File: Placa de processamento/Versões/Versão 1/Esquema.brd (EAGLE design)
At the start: 145.1 x 79.8 mm, 15 parts, among them IC2 5V

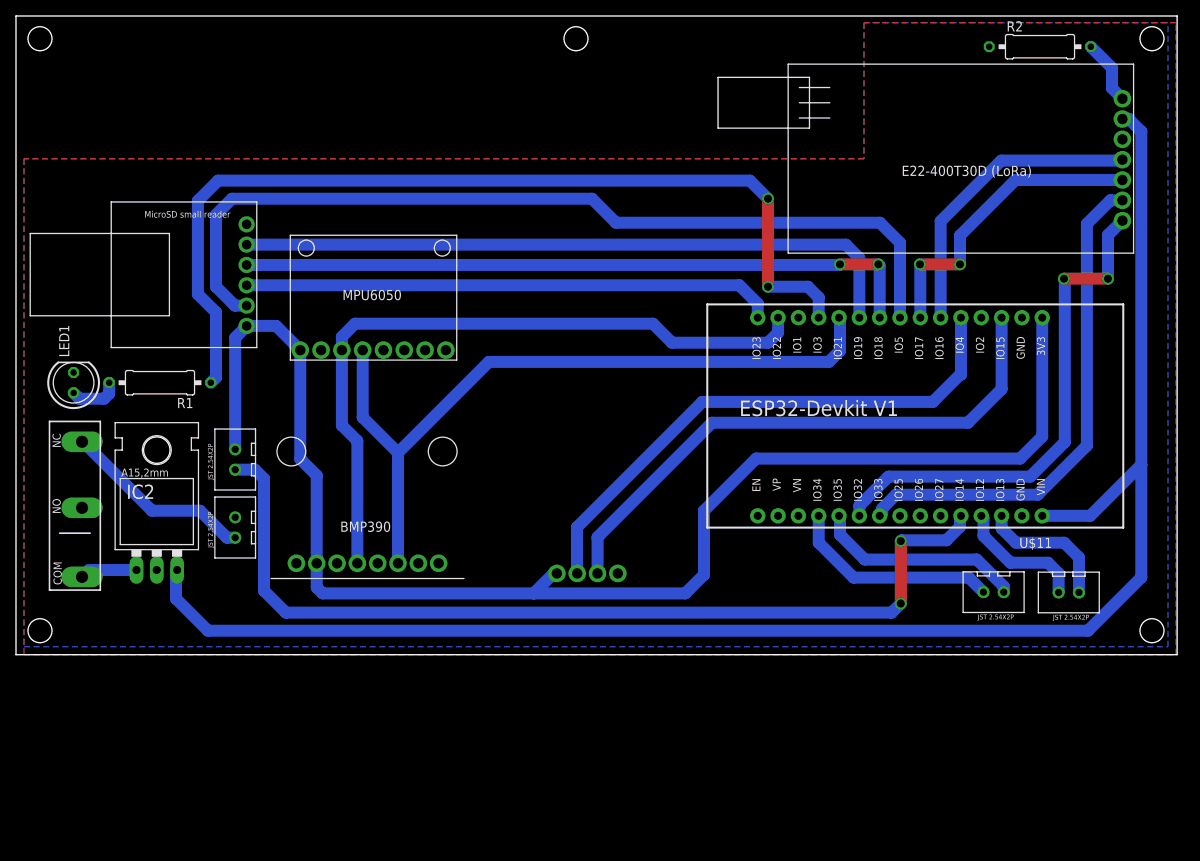
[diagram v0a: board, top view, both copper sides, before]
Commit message: mudanças na placa de processamento
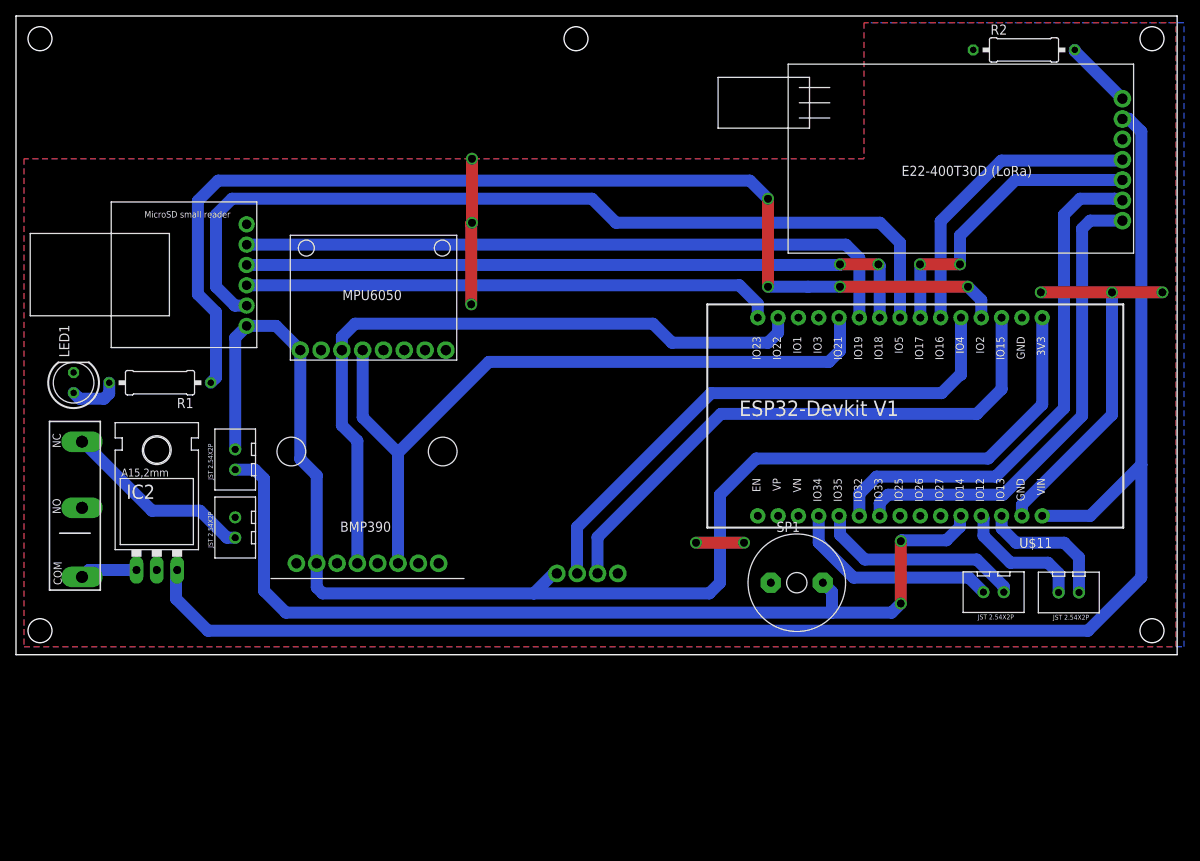
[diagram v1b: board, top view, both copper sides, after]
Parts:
- added SP1: AL60P, buzzer:AL60P
- R2: value 40R -> 46R
- moved R2 2.04 mm to (126.0, 75.6)
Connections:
- net BUZZER: now also SP1.2
- net GND: now also SP1.1, U$11.29
- net LED1: now also U$11.4; no longer U$11.12
- net M0: now also U$11.22; no longer U$11.21
- net M1: now also U$11.21; no longer U$11.22
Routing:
- net GND: track 0.00 -> 72.0 mm, vias 0 -> 8
- net LED1: track 117.6 -> 137.7 mm, vias 2 -> 4
- net BUZZER: track 116.6 -> 120.8 mm
- net M0: track 64.3 -> 60.3 mm, vias 2 -> 0
- net M1: track 63.3 -> 65.2 mm
- net 3V3: track 177.1 -> 176.5 mm

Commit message: teste
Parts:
- moved IC2 0.76 mm to (18.3, 14.1)
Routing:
- net VIN: track 7.16 -> 8.70 mm
- net V_BATTERY: track 24.1 -> 25.0 mm
- net VOUT: track 202.6 -> 201.9 mm
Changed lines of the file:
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@@
 <drawing>
 <settings>
-<setting alwaysvectorfont="no"/>
+<setting alwaysvectorfont="yes"/>
 <setting verticaltext="up"/>
 </settings>
@@
 </class>
 </classes>
-<designrules name="padronizacao do eagle *">
+<designrules name="default *">
 <description language="de">&lt;b&gt;EAGLE Design Rules&lt;/b&gt;
 &lt;p&gt;
@@
 <param name="msMicroVia" value="9.99mm"/>
 <param name="msBlindViaRatio" value="0.5"/>
-<param name="rvPadTop" value="0.35"/>
+<param name="rvPadTop" value="0.25"/>
 <param name="rvPadInner" value="0.25"/>
-<param name="rvPadBottom" value="0.35"/>
+<param name="rvPadBottom" value="0.25"/>
 <param name="rvViaOuter" value="0.25"/>
 <param name="rvViaInner" value="0.25"/>
 <param name="rvMicroViaOuter" value="0.25"/>
 <param name="rvMicroViaInner" value="0.25"/>
-<param name="rlMinPadTop" value="10mil"/>
+<param name="rlMinPadTop" value="20mil"/>
 <param name="rlMaxPadTop" value="30mil"/>
 <param name="rlMinPadInner" value="10mil"/>
 <param name="rlMaxPadInner" value="20mil"/>
-<param name="rlMinPadBottom" value="10mil"/>
+<param name="rlMinPadBottom" value="20mil"/>
 <param name="rlMaxPadBottom" value="30mil"/>
-<param name="rlMinViaOuter" value="8mil"/>
-<param name="rlMaxViaOuter" value="20mil"/>
-<param name="rlMinViaInner" value="8mil"/>
-<param name="rlMaxViaInner" value="20mil"/>
+<param name="rlMinViaOuter" value="22mil"/>
+<param name="rlMaxViaOuter" value="22mil"/>
+<param name="rlMinViaInner" value="10mil"/>
+<param name="rlMaxViaInner" value="10mil"/>
 <param name="rlMinMicroViaOuter" value="4mil"/>
 <param name="rlMaxMicroViaOuter" value="20mil"/>
@@
 <param name="srMinRoundness" value="0mil"/>
 <param name="srMaxRoundness" value="0mil"/>
-<param name="slThermalIsolate" value="10mil"/>
+<param name="slThermalIsolate" value="0mil"/>
 <param name="slThermalsForVias" value="0"/>
 <param name="dpMaxLengthDifference" value="10mm"/>
@@
 <attribute name="NAME" x="129.54" y="14.62" size="1.27" layer="21" rot="R180"/>
 </element>
-<element name="IC2" library="v-reg" library_urn="urn:adsk.eagle:library:409" package="78XXL" package3d_urn="urn:adsk.eagle:package:30361/1" value="5V" x="17.6" y="14.4" smashed="yes">
-<attribute name="NAME" x="13.79" y="19.48" size="1.778" layer="25" ratio="10"/>
-<attribute name="POPULARITY" value="10" x="17.6" y="14.4" size="1.778" layer="27" display="off"/>
-<attribute name="VALUE" x="13.663" y="16.94" size="1.778" layer="27" ratio="10"/>
+<element name="IC2" library="v-reg" library_urn="urn:adsk.eagle:library:409" package="78XXL" package3d_urn="urn:adsk.eagle:package:30361/1" value="5V" x="18.3" y="14.1" smashed="yes">
+<attribute name="NAME" x="14.49" y="19.18" size="1.778" layer="25" ratio="10"/>
+<attribute name="POPULARITY" value="10" x="18.3" y="14.1" size="1.778" layer="27" display="off"/>
+<attribute name="VALUE" x="14.363" y="16.64" size="1.778" layer="27" ratio="10"/>
 </element>
 <element name="LED1" library="led" library_urn="urn:adsk.eagle:library:259" package="LED5MM" package3d_urn="urn:adsk.eagle:package:15799/2" value="RED" x="7.2" y="34" smashed="yes" rot="R90">
@@
 <attribute name="VALUE" x="21.175" y="34.6858" size="1.27" layer="27" ratio="10" rot="R180"/>
 </element>
-<element name="U$12" library="CRD" library_urn="urn:adsk.eagle:library:39051337" package="CHAVESS-5GL" package3d_urn="urn:adsk.eagle:package:45208058/6" value="CHAVE_SS-5GL" x="8" y="19" smashed="yes" rot="R90"/>
+<element name="U$12" library="CRD" library_urn="urn:adsk.eagle:library:39051337" package="CHAVESS-5GL" package3d_urn="urn:adsk.eagle:package:45208058/14" value="CHAVE_SS-5GL" x="8" y="19" smashed="yes" rot="R90"/>
 <element name="R2" library="rcl" library_urn="urn:adsk.eagle:library:334" package="0309/12" package3d_urn="urn:adsk.eagle:package:23571/1" value="46R" x="126" y="75.6" smashed="yes">
 <attribute name="NAME" x="121.809" y="77.505" size="1.27" layer="25" ratio="10"/>
@@
 <contactref element="U$12" pad="P$1"/>
 <contactref element="IC2" pad="IN"/>
-<wire x1="8.254" y1="9.729" x2="9.115" y2="10.59" width="1.5" layer="16"/>
-<wire x1="9.115" y1="10.59" x2="15.06" y2="10.59" width="1.5" layer="16"/>
+<wire x1="7.238" y1="9.856" x2="10.856" y2="9.856" width="3.7" layer="16"/>
+<wire x1="11" y1="10" x2="10.856" y2="9.856" width="3.7" layer="16"/>
+<wire x1="15.76" y1="10.29" x2="15.47" y2="10" width="1.5" layer="16"/>
+<wire x1="15.47" y1="10" x2="11" y2="10" width="1.5" layer="16"/>
 </signal>
 <signal name="V_BATTERY">
 <contactref element="U$7" pad="1"/>
 <contactref element="U$12" pad="P$3"/>
-<wire x1="8.254" y1="26.62" x2="8.38" y2="26.62" width="1.5" layer="16"/>
-<wire x1="17" y1="18" x2="23" y2="18" width="1.5" layer="16"/>
 <wire x1="23" y1="18" x2="26.37" y2="14.63" width="1.5" layer="16"/>
 <wire x1="26.37" y1="14.63" x2="27.4" y2="14.63" width="1.5" layer="16"/>
-<wire x1="8.38" y1="26.62" x2="17" y2="18" width="1.5" layer="16"/>
+<wire x1="9.2385" y1="24.2385" x2="10.2385" y2="23.2385" width="1.5" layer="16"/>
+<wire x1="7.238" y1="26.239" x2="9.2385" y2="24.2385" width="3.7" layer="16"/>
+<wire x1="10.2385" y1="23.2385" x2="11.7615" y2="23.2385" width="1.5" layer="16"/>
+<wire x1="11.7615" y1="23.2385" x2="17" y2="18" width="1.5" layer="16"/>
+<wire x1="17" y1="18" x2="23" y2="18" width="1.5" layer="16"/>
 </signal>
 <signal name="GND">
@@
 <via x="128.1" y="45.3" extent="1-16" drill="1"/>
 <wire x1="137" y1="30" x2="137" y2="45.3" width="1.5" layer="16"/>
-<wire x1="137" y1="45.3" x2="143.3" y2="45.3" width="1.5" layer="1"/>
-<via x="143.3" y="45.3" extent="1-16" drill="1"/>
+<wire x1="137" y1="45.3" x2="143" y2="45.3" width="1.5" layer="1"/>
+<via x="143" y="45.3" extent="1-16" drill="1"/>
 </signal>
 <signal name="N$4">
@@
 <wire x1="140.666" y1="23.746" x2="140.666" y2="9.666" width="1.5" layer="16"/>
 <wire x1="140.666" y1="9.666" x2="134" y2="3" width="1.5" layer="16"/>
-<wire x1="134" y1="3" x2="24" y2="3" width="1.5" layer="16"/>
-<wire x1="24" y1="3" x2="20" y2="7" width="1.5" layer="16"/>
-<wire x1="20" y1="7" x2="20" y2="10.45" width="1.5" layer="16"/>
-<wire x1="20" y1="10.45" x2="20.14" y2="10.59" width="1.5" layer="16"/>
+<wire x1="24" y1="3" x2="134" y2="3" width="1.5" layer="16"/>
+<wire x1="20.84" y1="10.29" x2="20.84" y2="6.16" width="1.5" layer="16"/>
+<wire x1="20.84" y1="6.16" x2="24" y2="3" width="1.5" layer="16"/>
 </signal>
 <signal name="N$7">

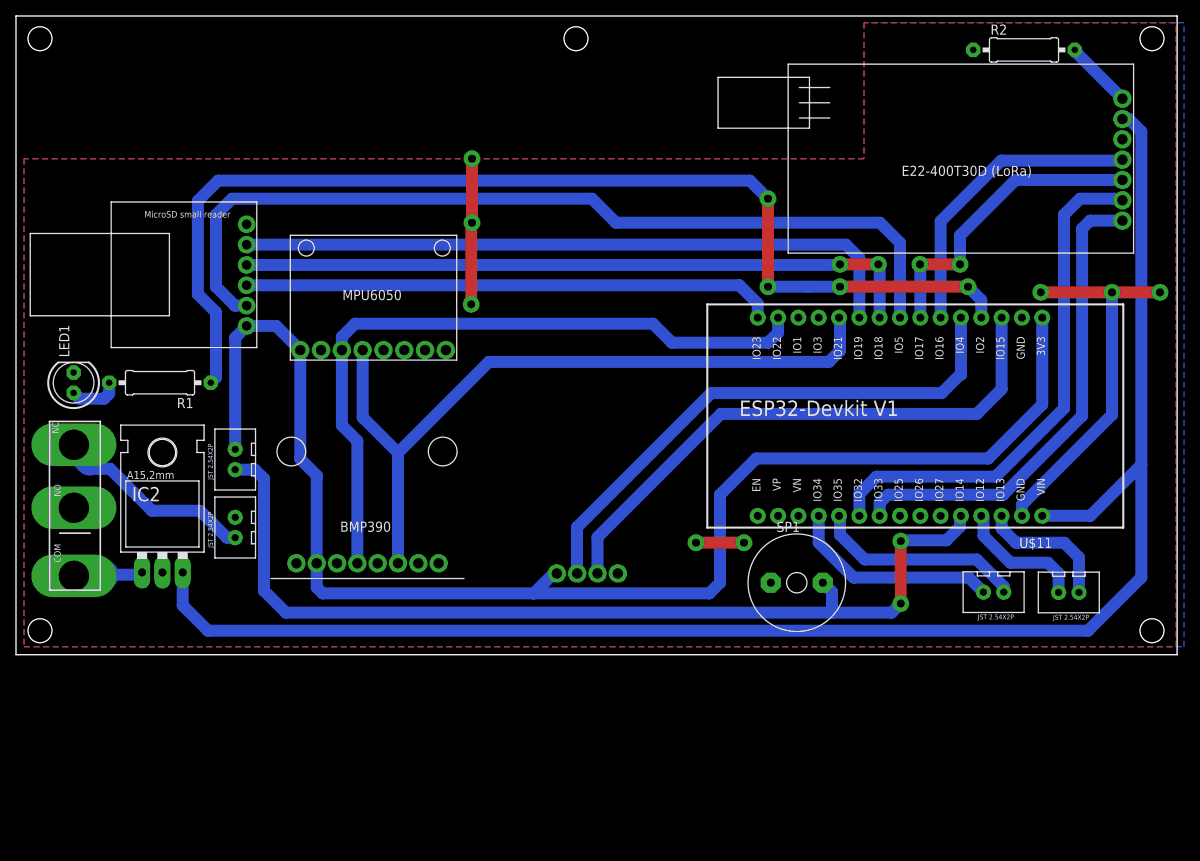
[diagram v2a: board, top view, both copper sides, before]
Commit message: atualização de regulador
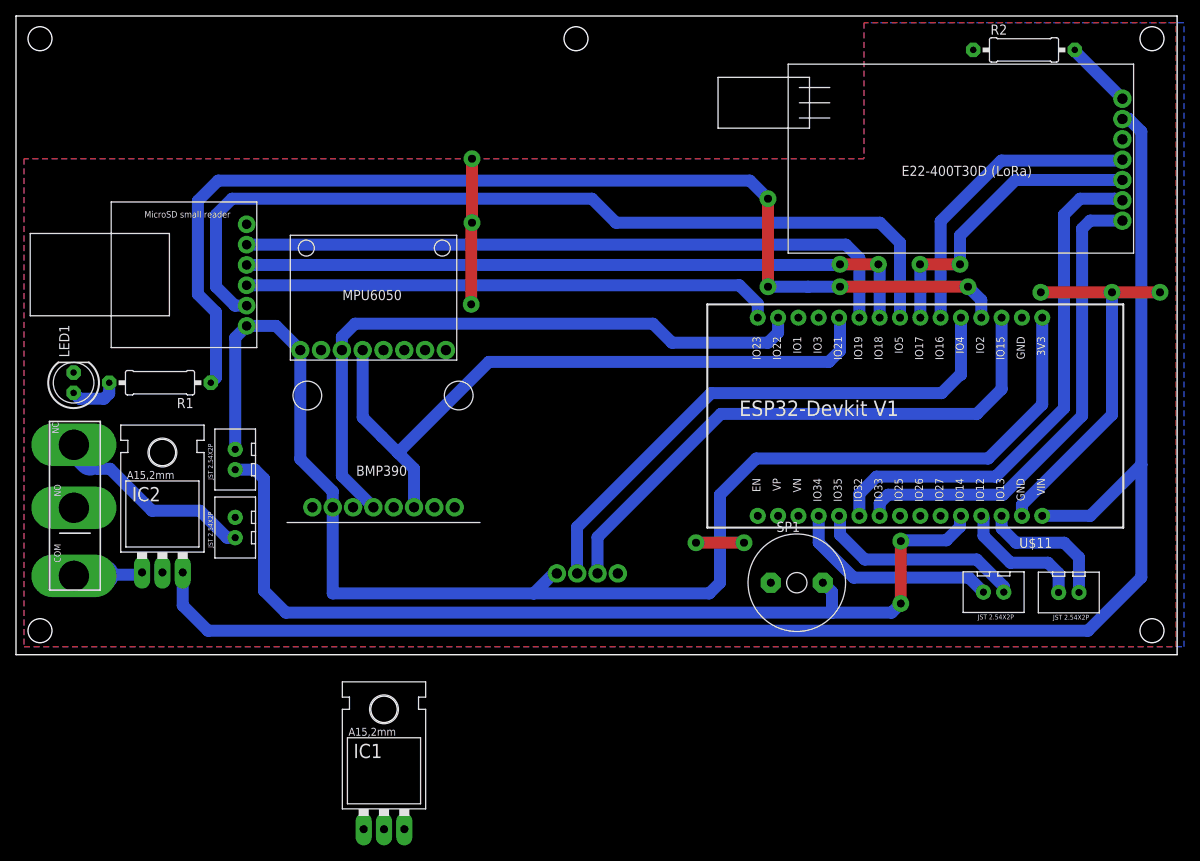
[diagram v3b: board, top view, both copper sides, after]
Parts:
- added IC1: 5V, v-reg:78XXL
- moved U$1 7.28 mm to (45.6, 26.8)
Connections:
- new net VOUT_LORA: IC1.OUT, U$2.VCC
- net GND: now also IC1.GND
- net VIN: now also IC1.IN
- net VOUT: no longer U$2.VCC
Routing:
- net SDA: track 93.2 -> 87.0 mm
- net SCL: track 87.7 -> 81.5 mm
- net 3V3: track 176.5 -> 175.8 mm
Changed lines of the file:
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@@
 </autorouter>
 <elements>
-<element name="U$1" library="CRD" library_urn="urn:adsk.eagle:library:39051337" package="BMP390_FOOTPRINT" package3d_urn="urn:adsk.eagle:package:40965124/5" value="BMP390V1" x="43.561" y="19.812" smashed="yes"/>
+<element name="U$1" library="CRD" library_urn="urn:adsk.eagle:library:39051337" package="BMP390_FOOTPRINT" package3d_urn="urn:adsk.eagle:package:40965124/5" value="BMP390V1" x="45.561" y="26.812" smashed="yes"/>
 <element name="U$2" library="CRD" library_urn="urn:adsk.eagle:library:39051337" package="E22-400T30D_FOOTPRINT" package3d_urn="urn:adsk.eagle:package:40965099/5" value="E22-400T30D" x="121.92" y="63.66" smashed="yes" rot="R180"/>
 <element name="U$3" library="CRD" library_urn="urn:adsk.eagle:library:39051337" package="GPS_MODULE_FOOTPRINT" package3d_urn="urn:adsk.eagle:package:39608400/7" value="GPS_MODULE" x="71.22" y="26.67" smashed="yes" rot="MR0"/>
@@
 <attribute name="VALUE" x="93.7138" y="5.19" size="1.27" layer="27" ratio="10"/>
 </element>
+<element name="IC1" library="v-reg" library_urn="urn:adsk.eagle:library:409" package="78XXL" package3d_urn="urn:adsk.eagle:package:30361/1" value="5V" x="46" y="-18" smashed="yes">
+<attribute name="NAME" x="42.19" y="-12.92" size="1.778" layer="25" ratio="10"/>
+<attribute name="POPULARITY" value="10" x="46" y="-18" size="1.778" layer="27" display="off"/>
+<attribute name="VALUE" x="42.063" y="-15.46" size="1.778" layer="27" ratio="10"/>
+</element>
 </elements>
 <signals>
@@
 <wire x1="15.76" y1="10.29" x2="15.47" y2="10" width="1.5" layer="16"/>
 <wire x1="15.47" y1="10" x2="11" y2="10" width="1.5" layer="16"/>
+<contactref element="IC1" pad="IN"/>
+<wire x1="7.238" y1="9.856" x2="43.46" y2="-21.81" width="0" layer="19" extent="1-1"/>
 </signal>
 <signal name="V_BATTERY">
@@
 <wire x1="137" y1="45.3" x2="143" y2="45.3" width="1.5" layer="1"/>
 <via x="143" y="45.3" extent="1-16" drill="1"/>
+<contactref element="IC1" pad="GND"/>
+<wire x1="128.1" y1="45.3" x2="119.65" y2="75.6" width="0" layer="19" extent="1-1"/>
+<wire x1="125.74" y1="42.13" x2="128.1" y2="45.3" width="0" layer="19" extent="1-1"/>
+<wire x1="94.3488" y1="9" x2="125.74" y2="17.36" width="0" layer="19" extent="1-1"/>
+<wire x1="91" y1="14" x2="94.3488" y2="9" width="0" layer="19" extent="1-1"/>
+<wire x1="75.23" y1="10.16" x2="85" y2="14" width="0" layer="19" extent="1-1"/>
+<wire x1="42.132" y1="18.43" x2="75.23" y2="10.16" width="0" layer="19" extent="1-1"/>
+<wire x1="27.4" y1="17.17" x2="42.132" y2="18.43" width="0" layer="19" extent="1-1"/>
+<wire x1="18.3" y1="10.29" x2="27.4" y2="17.17" width="0" layer="19" extent="1-1"/>
+<wire x1="38.1355" y1="38.0755" x2="27.4" y2="17.17" width="0" layer="19" extent="1-1"/>
+<wire x1="28.829" y1="53.8" x2="38.1355" y2="38.0755" width="0" layer="19" extent="1-1"/>
+<wire x1="56.9" y1="43.8" x2="38.1355" y2="38.0755" width="0" layer="19" extent="1-1"/>
+<wire x1="7.2" y1="35.27" x2="27.4" y2="17.17" width="0" layer="19" extent="1-1"/>
+<wire x1="46" y1="-21.81" x2="18.3" y2="10.29" width="0" layer="19" extent="1-1"/>
 </signal>
 <signal name="N$4">
@@
 <contactref element="U$11" pad="30"/>
 <contactref element="IC2" pad="OUT"/>
-<contactref element="U$2" pad="VCC"/>
 <wire x1="139.1" y1="66.9667875" x2="139.1" y2="67" width="1.5" layer="16"/>
 <wire x1="140.666" y1="65.4007875" x2="139.1" y2="66.9667875" width="1.5" layer="16"/>
@@
 <wire x1="140.666" y1="65.4007875" x2="140.666" y2="23.746" width="1.5" layer="16"/>
 <wire x1="139.1" y1="67" x2="138.341" y2="67" width="1.5" layer="16"/>
-<wire x1="138.341" y1="67" x2="138.303" y2="66.962" width="1.5" layer="16"/>
 <wire x1="140.666" y1="23.746" x2="140.666" y2="9.666" width="1.5" layer="16"/>
 <wire x1="140.666" y1="9.666" x2="134" y2="3" width="1.5" layer="16"/>
@@
 <wire x1="27.4" y1="39.622" x2="28.8535" y2="41.0755" width="1.5" layer="16"/>
 <wire x1="35.5355" y1="24.4645" x2="35.5355" y2="38.0755" width="1.5" layer="16"/>
-<wire x1="37.592" y1="11.43" x2="37.592" y2="22.408" width="1.5" layer="16"/>
-<wire x1="37.592" y1="22.408" x2="35.5355" y2="24.4645" width="1.5" layer="16"/>
-<wire x1="37.592" y1="11.43" x2="37.592" y2="8.408" width="1.5" layer="16"/>
+<wire x1="39.592" y1="18.43" x2="39.592" y2="20.408" width="1.5" layer="16"/>
+<wire x1="39.592" y1="20.408" x2="35.5355" y2="24.4645" width="1.5" layer="16"/>
+<wire x1="39.592" y1="18.43" x2="39.592" y2="7.662" width="1.5" layer="16"/>
 <wire x1="67.61" y1="10.16" x2="67.21" y2="10.16" width="1.5" layer="16"/>
 <wire x1="67.21" y1="10.16" x2="64.712" y2="7.662" width="1.5" layer="16"/>
-<wire x1="37.592" y1="8.408" x2="38.338" y2="7.662" width="1.5" layer="16"/>
-<wire x1="38.338" y1="7.662" x2="64.712" y2="7.662" width="1.5" layer="16"/>
+<wire x1="39.592" y1="7.662" x2="64.712" y2="7.662" width="1.5" layer="16"/>
 <wire x1="64.712" y1="7.662" x2="86.662" y2="7.662" width="1.5" layer="16"/>
 <wire x1="86.662" y1="7.662" x2="88" y2="9" width="1.5" layer="16"/>
@@
 <contactref element="U$1" pad="SCL"/>
 <contactref element="U$9" pad="SCL"/>
-<wire x1="42.672" y1="11.43" x2="42.672" y2="26.728" width="1.5" layer="16"/>
-<wire x1="40.7355" y1="28.6645" x2="40.7355" y2="38.0755" width="1.5" layer="16"/>
-<wire x1="42.672" y1="26.728" x2="40.7355" y2="28.6645" width="1.5" layer="16"/>
+<wire x1="40.7355" y1="38.0755" x2="40.7355" y2="22.3665" width="1.5" layer="16"/>
+<wire x1="44.672" y1="18.43" x2="40.7355" y2="22.3665" width="1.5" layer="16"/>
 <wire x1="40.7355" y1="38.0755" x2="40.7355" y2="39.7355" width="1.5" layer="16"/>
 <wire x1="40.7355" y1="39.7355" x2="42.378" y2="41.378" width="1.5" layer="16"/>
@@
 <contactref element="U$1" pad="SDA"/>
 <contactref element="U$9" pad="SDA"/>
-<wire x1="47.752" y1="11.43" x2="47.752" y2="25.248" width="1.5" layer="16"/>
+<wire x1="49.752" y1="18.43" x2="49.752" y2="23.248" width="1.5" layer="16"/>
 <wire x1="43.3355" y1="29.6645" x2="43.3355" y2="38.0755" width="1.5" layer="16"/>
-<wire x1="47.752" y1="25.248" x2="43.3355" y2="29.6645" width="1.5" layer="16"/>
+<wire x1="47.752" y1="25.248" x2="45.752" y2="27.248" width="1.5" layer="16"/>
+<wire x1="49.752" y1="23.248" x2="47.752" y2="25.248" width="1.5" layer="16"/>
+<wire x1="45.752" y1="27.248" x2="43.3355" y2="29.6645" width="1.5" layer="16"/>
 <wire x1="47.752" y1="25.248" x2="59.104" y2="36.6" width="1.5" layer="16"/>
 <wire x1="101.6" y1="36.6" x2="103" y2="38" width="1.5" layer="16"/>
@@
 <wire x1="104.702" y1="9.638" x2="119.112" y2="9.638" width="1.5" layer="16"/>
 </signal>
+<signal name="VOUT_LORA">
+<contactref element="IC1" pad="OUT"/>
+<contactref element="U$2" pad="VCC"/>
+<wire x1="48.54" y1="-21.81" x2="138.303" y2="66.962" width="0" layer="19" extent="1-1"/>
+</signal>
 </signals>
